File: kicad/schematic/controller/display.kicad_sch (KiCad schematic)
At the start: 13 parts, among them U4 ILI9341

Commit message: feat(pcb): pcb wip
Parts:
- J3: value ~ -> 01x06; footprint (none) -> connector:Pin_01x06
- J4: value ~ -> 01x02; footprint (none) -> connector:Pin_01x02
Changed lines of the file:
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@@
 			)
 		)
-		(property "Value" "~"
+		(property "Value" "01x06"
 			(at 143.51 139.31 0)
 			(effects
@@
 			)
 		)
-		(property "Footprint" ""
+		(property "Footprint" "connector:Pin_01x06"
 			(at 143.51 130.81 0)
 			(effects
@@
 			)
 		)
-		(property "Value" "~"
+		(property "Value" "01x02"
 			(at 128.27 100.02 0)
 			(effects
@@
 			)
 		)
-		(property "Footprint" ""
+		(property "Footprint" "connector:Pin_01x02"
 			(at 128.27 96.52 0)
 			(effects

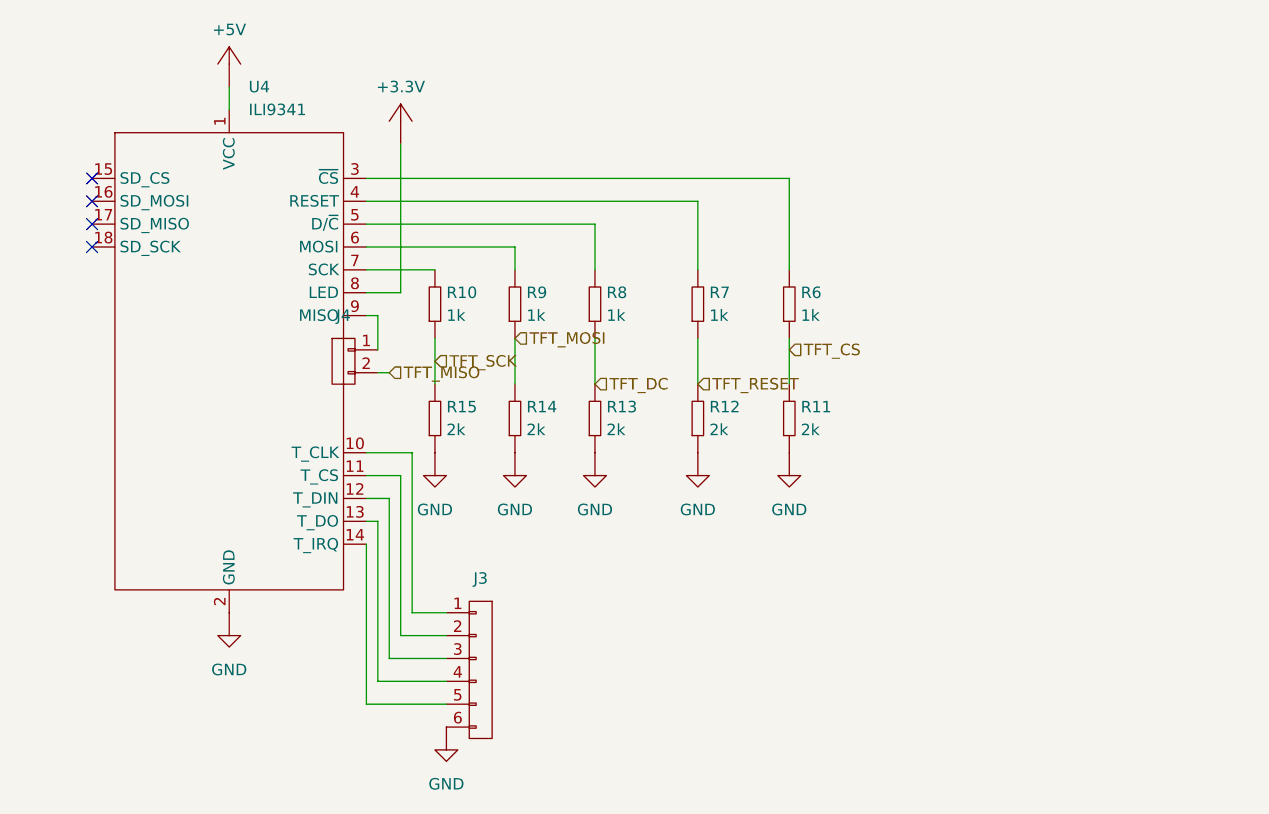
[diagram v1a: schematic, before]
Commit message: feat(schematic): cleanup controller
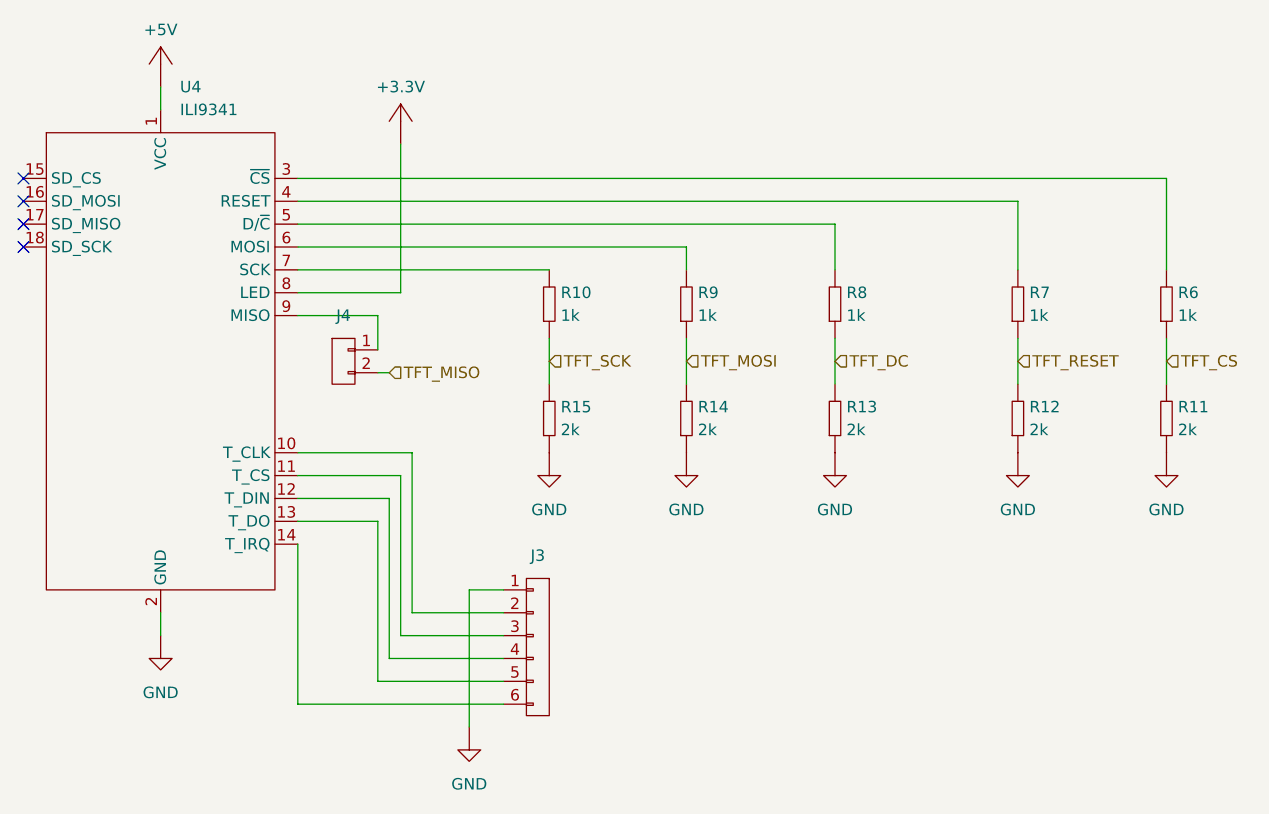
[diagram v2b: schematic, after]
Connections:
- net GND: now also J3.1; no longer J3.6
- net at U4.10 (T_CLK): now also J3.2; no longer J3.1
- net at U4.11 (T_CS): now also J3.3; no longer J3.2
- net at U4.12 (T_DIN): now also J3.4; no longer J3.3
- net at U4.13 (T_DO): now also J3.5; no longer J3.4
- net at U4.14 (T_IRQ): now also J3.6; no longer J3.5
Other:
- moved on the sheet: J3, R10, R11, R12, R13, R14, R15, R6, R7, R8, R9, U4

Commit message: update controller pcb
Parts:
- R10, R6, R7, R8, R9: Ext. Price (none) -> 0.07; LCSC Part (none) -> C2907113; Manufacturer (none) -> FOJAN; Manufacturer Part (none) -> FRC0603J102 TS; Unit Price (none) -> 0.0007
- R11, R12, R13, R14, R15: Ext. Price (none) -> 0.09; LCSC Part (none) -> C2907022; Manufacturer (none) -> FOJAN; Manufacturer Part (none) -> FRC0603F2001TS; Unit Price (none) -> 0.0009
